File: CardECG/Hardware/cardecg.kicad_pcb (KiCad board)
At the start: 2 copper layers, 57 parts, among them CN1 2TAP, P1 PROG, P2 BATTERY, Q1 TSM2311CX, Q2 NTR1P02T1, Q3 TSM2311CX, Q4 TSM2311CX, Q5 NMOS_GSD, Q6 NMOS_GSD, Q7 TSM2311CX, Q8 TSM2311CX, U1 LMV341, U2 TPS71725, U3 ADuC7061, U4 SSD1306, U6 DNP, U7 DNP

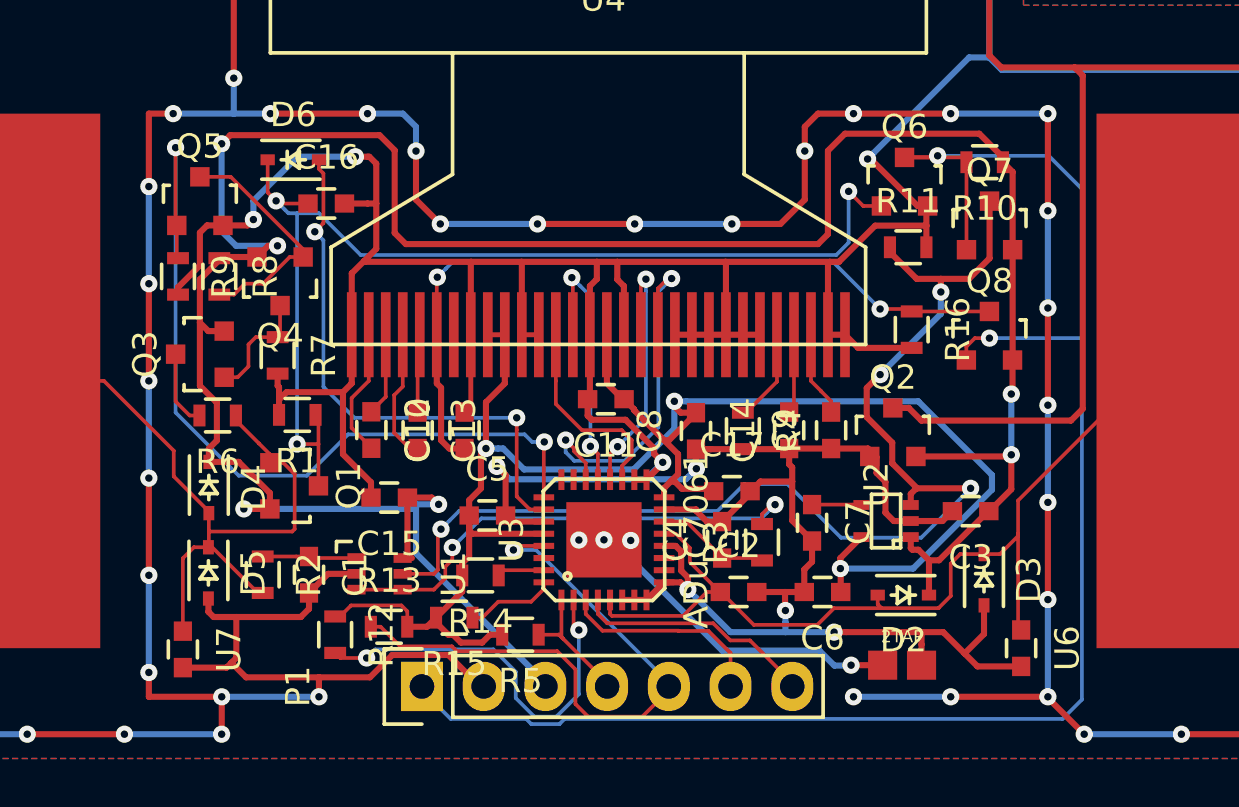
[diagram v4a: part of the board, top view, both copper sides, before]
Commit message: EMC optimizations. Compoments rearranged to leave more space for the upper PCB.
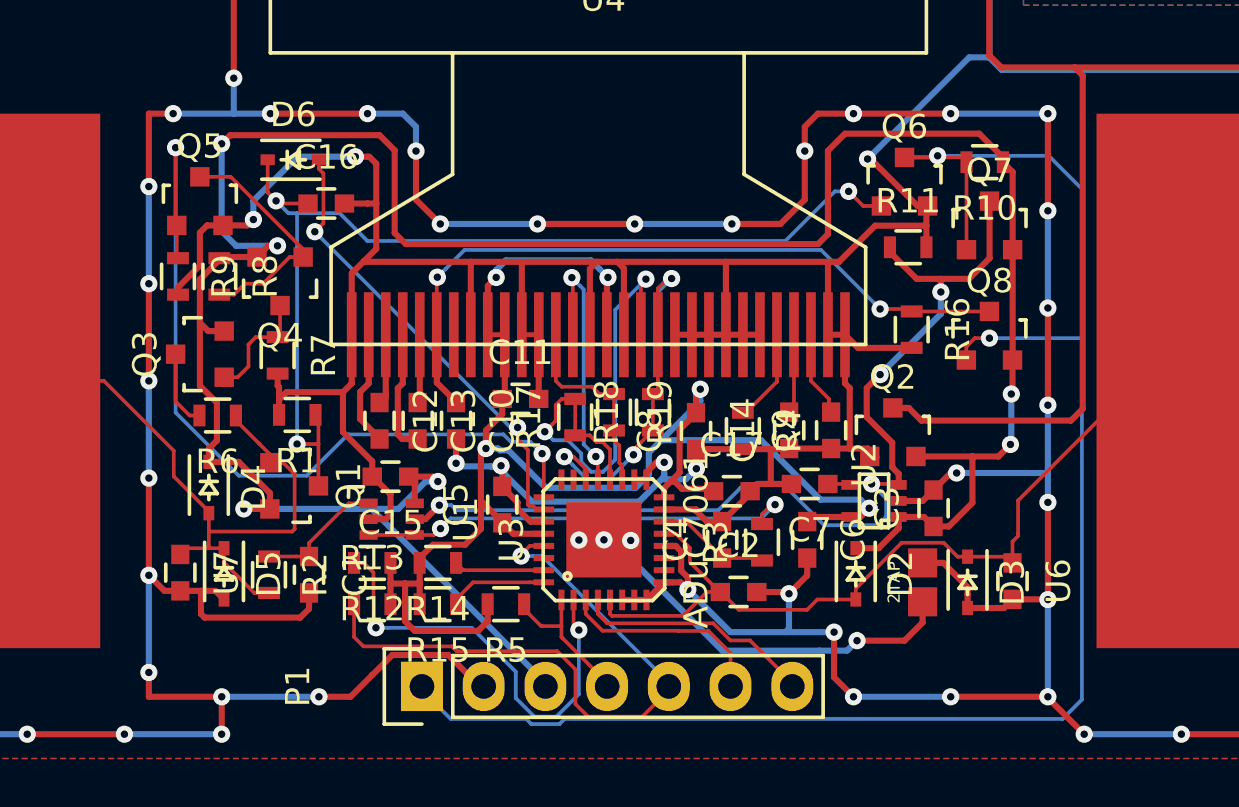
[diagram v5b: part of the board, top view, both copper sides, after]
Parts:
- added R17: 49, Resistors_SMD:R_0603, F.Cu at (67.5, 63.0)
- added R18: 49, Resistors_SMD:R_0603, F.Cu at (70.8, 62.8)
- added R19: 49, Resistors_SMD:R_0603, F.Cu at (69.2, 62.8)
- R1, R10, R11, R16, R8, R9: value 100k -> 47k
- R13: value 47k -> 3.9k
- R5: value 3.9k -> 47k
- moved C11 3.51 mm to (65.3, 62.2), turned to 0 degrees
- moved CN1 3.51 mm to (81.8, 69.8), turned to 90 degrees
- moved R12 3.33 mm to (59.2, 69.0), turned to 180 degrees
- moved U7 3.16 mm to (51.3, 69.3)
- moved U6 2.78 mm to (85.5, 69.7)
- moved U1 2.30 mm to (60.0, 67.2)
- moved C6 2.24 mm to (77.1, 68.0), turned to 270 degrees
- moved D2 2.14 mm to (79.1, 69.4), turned to 270 degrees
- moved R14 1.83 mm to (61.9, 69.0)
- moved C7 1.60 mm to (77.2, 65.7), turned to 180 degrees
- moved C3 1.53 mm to (82.3, 66.7), turned to 90 degrees
- moved R5 1.39 mm to (64.7, 70.7)
- moved R13 1.16 mm to (59.2, 70.7)
- moved U2 0.96 mm to (79.8, 66.4)
- moved R15 0.87 mm to (61.9, 70.7)
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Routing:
- net Net-(R17-Pad1): track 11.2 -> 20.9 mm
- net GND: track 587.4 -> 578.3 mm, vias 91 -> 93
- net VCC: track 48.5 -> 41.5 mm
- net VDD: track 74.0 -> 67.9 mm, vias 3 -> 5
- net Net-(C2-Pad1): track 48.9 -> 44.4 mm
- net POWER_ON: track 22.8 -> 19.0 mm
- net Net-(CN1-Pad1): track 15.8 -> 18.7 mm
- net Net-(R3-Pad2): track 20.7 -> 18.3 mm
- net Net-(D4-Pad2): track 34.6 -> 32.5 mm
- net Net-(R18-Pad1): track 16.0 -> 14.1 mm, vias 2 -> 3
- net Net-(C1-Pad1): track 3.50 -> 5.42 mm
- net Net-(R14-Pad1): track 1.95 -> 3.73 mm
- net Net-(R12-Pad2): track 16.4 -> 18.1 mm
- net Net-(C16-Pad1): track 45.2 -> 43.5 mm
- net +BATT: track 111.6 -> 110.1 mm
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
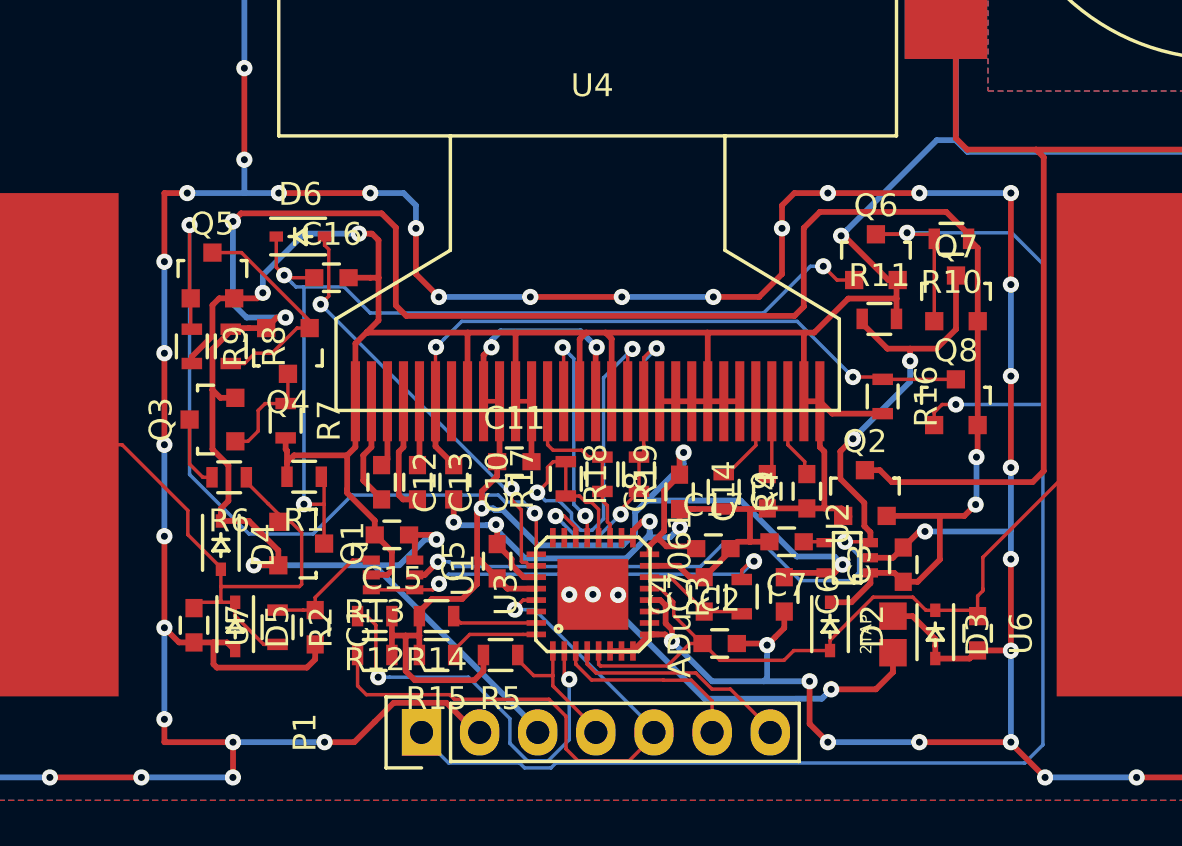
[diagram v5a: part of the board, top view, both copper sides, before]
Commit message: Change transistors to smaller package.
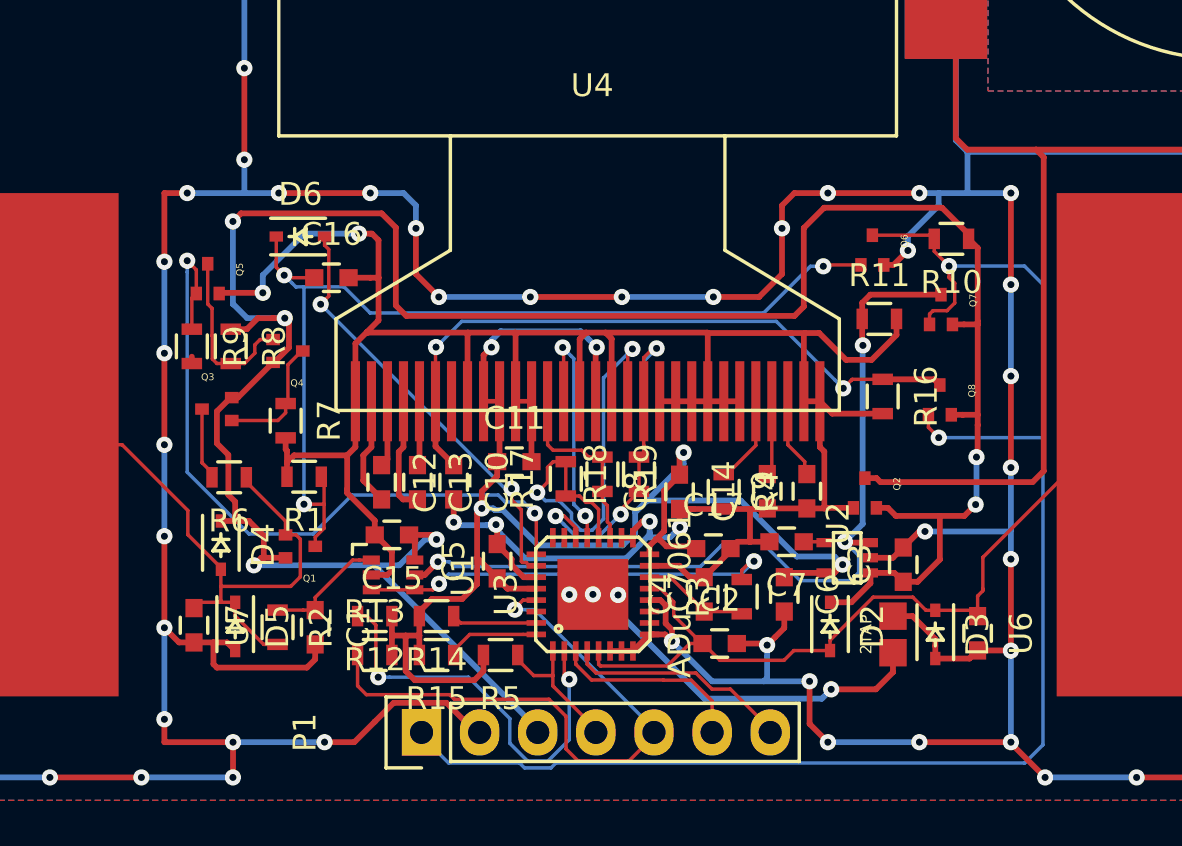
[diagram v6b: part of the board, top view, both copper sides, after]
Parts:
- Q1, Q3, Q4, Q7, Q8: value TSM2311CX -> NX3008PBKT; footprint TO_SOT_Packages_SMD:SOT-23 -> mod:SOT416
- Q2: value NTR1P02T1 -> NX3008PBKT; footprint TO_SOT_Packages_SMD:SOT-23 -> mod:SOT416
- Q5, Q6: value NMOS_GSD -> NX3008NBKT; footprint TO_SOT_Packages_SMD:SOT-23 -> mod:SOT416
- U2: value TPS71725 -> LD6815TD/25P
- moved Q7 0.82 mm to (84.0, 55.5), turned to 270 degrees
- moved Q8 0.71 mm to (83.9, 59.5), turned to 270 degrees
- moved Q3 0.50 mm to (52.3, 59.9), turned to 0 degrees
- moved Q6 0.35 mm to (81.0, 53.0), turned to 270 degrees
- moved Q5 0.25 mm to (51.9, 54.2), turned to 270 degrees
- moved Q1 0.13 mm to (56.0, 65.9), turned to 180 degrees
- turned Q2 to 270 degrees
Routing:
- net GND: track 578.3 -> 570.7 mm
- net +BATT: track 110.1 -> 113.3 mm
- net VCC: track 41.5 -> 38.4 mm, vias 4 -> 3
- net PULLUP_OFF: track 34.5 -> 31.7 mm
- net ~FORCE_ON: track 69.1 -> 66.7 mm
- net Net-(Q4-Pad1): track 9.89 -> 7.63 mm
- net Net-(Q3-Pad1): track 4.75 -> 5.54 mm

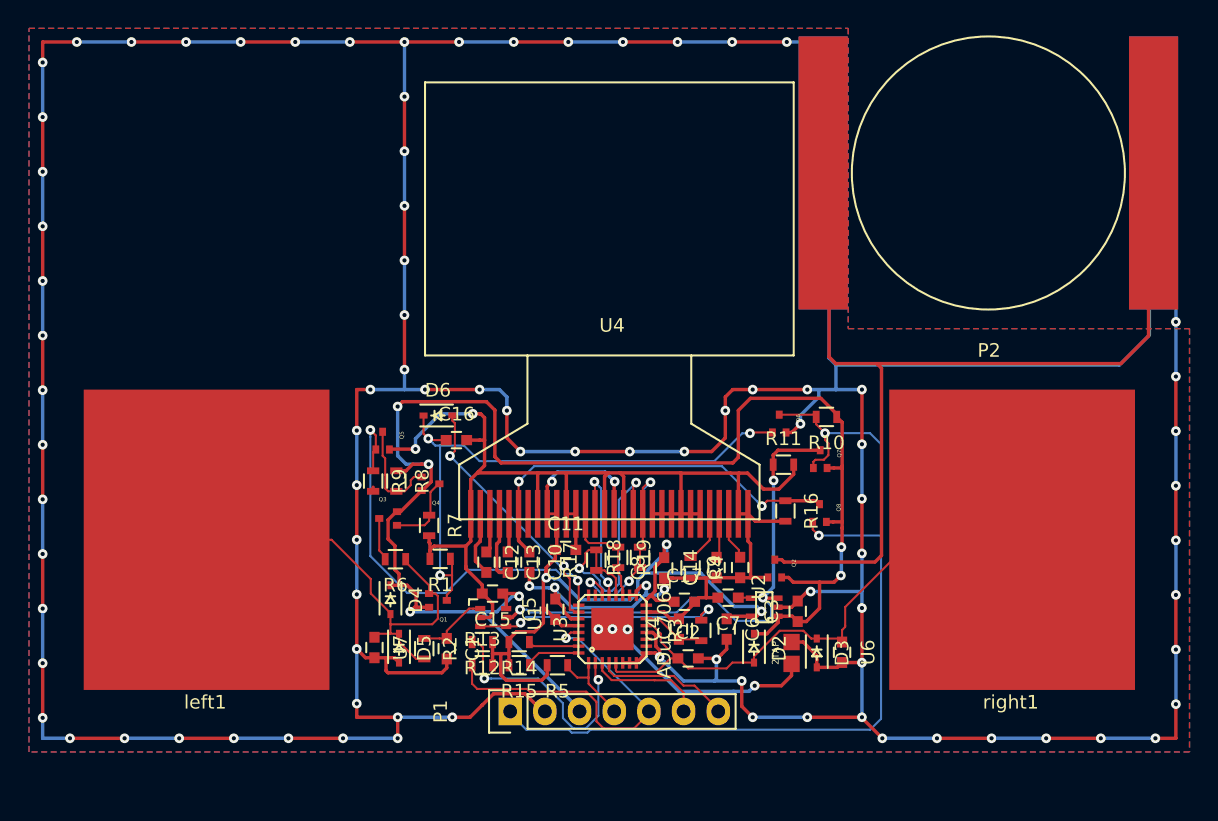
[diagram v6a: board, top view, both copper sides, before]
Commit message: Add filter cap, pulldown resistor, battery ESD protection.
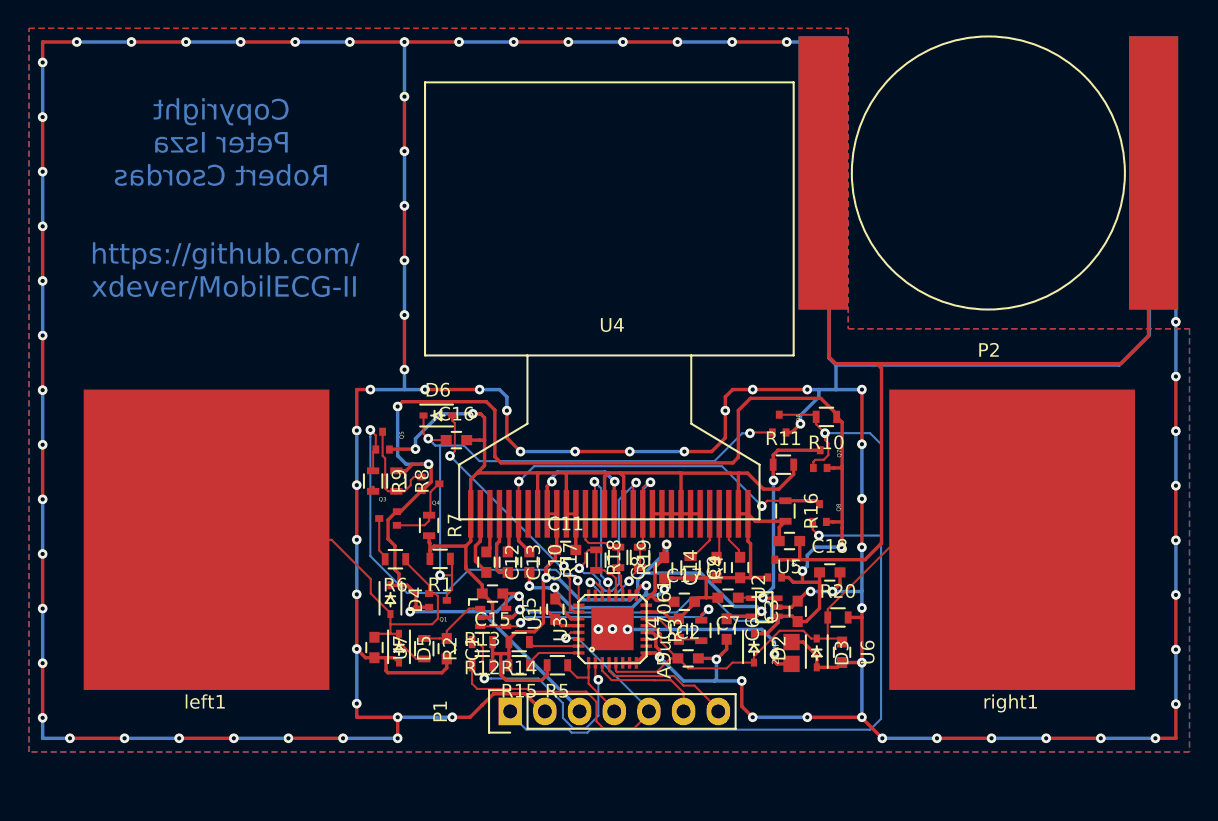
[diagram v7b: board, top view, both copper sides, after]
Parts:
- added C18: 1uF, Capacitors_SMD:C_0603, F.Cu at (84.7, 63.9)
- added R20: 47k, Resistors_SMD:R_0603, F.Cu at (85.2, 67.2)
- added U5: DNP, Capacitors_SMD:C_0603, F.Cu at (81.7, 61.5)
- C2: value C -> 100nF
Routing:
- net Net-(C2-Pad1): track 44.4 -> 52.6 mm
- net GND: track 570.7 -> 574.9 mm, vias 93 -> 94
- net Net-(CN1-Pad1): track 18.7 -> 16.3 mm
- net +BATT: track 113.3 -> 114.9 mm
- net Net-(P2-Pad1): track 76.5 -> 77.2 mm
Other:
- board text added: "Copyright Peter Isza Robert Csordas"
- board text added: "https://github.com/ xdever/MobilECG-II"

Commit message: Random modifications.
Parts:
- removed C7: 10nF, Capacitors_SMD:C_0603
- removed D2, D3, D4, D5: D, Diodes_SMD:SOD-323
- removed Q8: NX3008PBKT, mod:SOT416
- added R21: 3.9k, Resistors_SMD:R_0603, F.Cu at (82.4, 70.0)
- added R22: 3.9k, Resistors_SMD:R_0603, F.Cu at (56.8, 66.8)
- C1: value 127pF -> 100pF
- C4: value 100nF -> 8.2nF NP0
- R16: value 47k -> 49
- R3: value 3.9k -> 47k
- R6, R7: value 20M -> 10M
- U2: value LD6815TD/25P -> LD6805K/25; footprint TO_SOT_Packages_SMD:SC-70-5 -> mod:DFN1010C-4
- U5, U6, U7: value DNP -> TPD1E10B06; footprint Capacitors_SMD:C_0603 -> Capacitors_SMD:C_0402
- moved R1 28.5 mm to (84.6, 64.5), turned to 0 degrees
- moved D6 26.2 mm to (81.5, 58.0), turned to 180 degrees
- moved R16 17.0 mm to (65.1, 64.3)
- moved C16 16.6 mm to (56.0, 70.7), turned to 180 degrees
- moved R11 11.8 mm to (84.8, 67.2), turned to 90 degrees
- moved R10 11.0 mm to (82.5, 63.3), turned to 270 degrees
- moved Q6 10.2 mm to (84.6, 62.5), turned to 0 degrees
- moved C2 8.87 mm to (82.4, 66.6), turned to 180 degrees
- moved Q7 8.77 mm to (80.2, 63.5), turned to 0 degrees
- moved Q5 5.59 mm to (53.3, 59.6), turned to 0 degrees
- moved C18 5.22 mm to (80.7, 60.5), turned to 90 degrees
- moved Q3 5.12 mm to (53.8, 64.8)
- moved R8 5.08 mm to (53.0, 62.2), turned to 90 degrees
- moved R9 5.05 mm to (55.5, 59.8), turned to 90 degrees
- moved Q4 5.03 mm to (55.1, 62.4)
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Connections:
- C10 pad 1: OLED_PWR -> VCC
- C15 pad 1: +BATT -> GND
- C15 pad 2: GND -> +BATT
- C3 pad 1: +BATT -> VCC
- C6 pad 1: VDD -> GND
- C6 pad 2: GND -> VDD
- D6 pad 2: POWER_ON -> RX/POWER_ON
- P1 pad 1: ~FORCE_ON -> GND
- P1 pad 2: GND -> ~PROG
- P1 pad 3: +BATT -> ~RESET
- P1 pad 4: ~RESET -> RX/POWER_ON
- P1 pad 5: ~PROG -> TX
- P1 pad 6: RX -> +BATT
- P1 pad 7: TX -> ~FORCE_ON
- Q1 pad 1: Net-(D4-Pad2) -> Net-(C1-Pad1)
- R11 pad 1: VCC -> Net-(C2-Pad1)
- R11 pad 2: GND -> Net-(R11-Pad2)
- R16 pad 1: OLED_PWR -> Net-(R16-Pad1)
- R16 pad 2: GND -> Net-(R16-Pad1)
- R2 pad 2: Net-(D4-Pad2) -> Net-(R2-Pad2)
- R20 pad 1: Net-(C2-Pad1) -> Net-(R20-Pad1)
- R6 pad 1: Net-(D4-Pad2) -> Net-(C1-Pad1)
- U1 pad 1: Net-(C1-Pad1) -> Net-(R22-Pad1)
- U2 pad 1: +BATT -> VDD
- U2 pad 4: Net-(C7-Pad1) -> VCC
- U3 pad 13: Net-(C2-Pad1) -> Net-(R20-Pad1)
- U3 pad 26: POWER_ON -> Net-(R16-Pad1)
- U3 pad 3: RX -> RX/POWER_ON
- U3 pad 5: Net-(C2-Pad1) -> Net-(R20-Pad1)
- U4 pad 10: VDD -> GND
- U4 pad 15: GND -> Net-(R16-Pad1)
- U4 pad 6: OLED_PWR -> VCC
- U7 pad 1: Net-(D4-Pad2) -> Net-(C1-Pad1)
- left1 pad 1: Net-(D4-Pad2) -> Net-(R2-Pad2)
- right1 pad 1: Net-(C2-Pad1) -> Net-(R11-Pad2)
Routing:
- net +BATT: track 114.9 -> 62.1 mm, vias 6 -> 4
- net ~FORCE_ON: track 66.7 -> 18.2 mm, vias 2 -> 3
- net Net-(C2-Pad1): track 52.6 -> 6.77 mm
- net RX/POWER_ON: track 0.00 -> 36.5 mm, vias 0 -> 3
- net Net-(D4-Pad2): track 32.2 -> 0.00 mm
- net OLED_PWR: track 31.2 -> 0.00 mm, vias 2 -> 0
- net GND: track 574.9 -> 549.8 mm, vias 94 -> 89
- net Net-(R20-Pad1): track 0.00 -> 20.6 mm
- net POWER_ON: track 19.0 -> 0.00 mm, vias 2 -> 0
- net Net-(R2-Pad2): track 0.00 -> 15.4 mm
- net Net-(R11-Pad2): track 0.00 -> 15.3 mm
- net PULLUP_OFF: track 31.7 -> 16.8 mm
- net ~PROG: track 26.6 -> 15.4 mm
- net Net-(R16-Pad1): track 0.00 -> 10.6 mm
- net Net-(P2-Pad1): track 77.2 -> 67.2 mm
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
